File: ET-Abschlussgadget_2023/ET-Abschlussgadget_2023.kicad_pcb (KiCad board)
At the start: 2 copper layers, 85 x 54 mm, 14 parts, among them U1 ATtiny10-TS

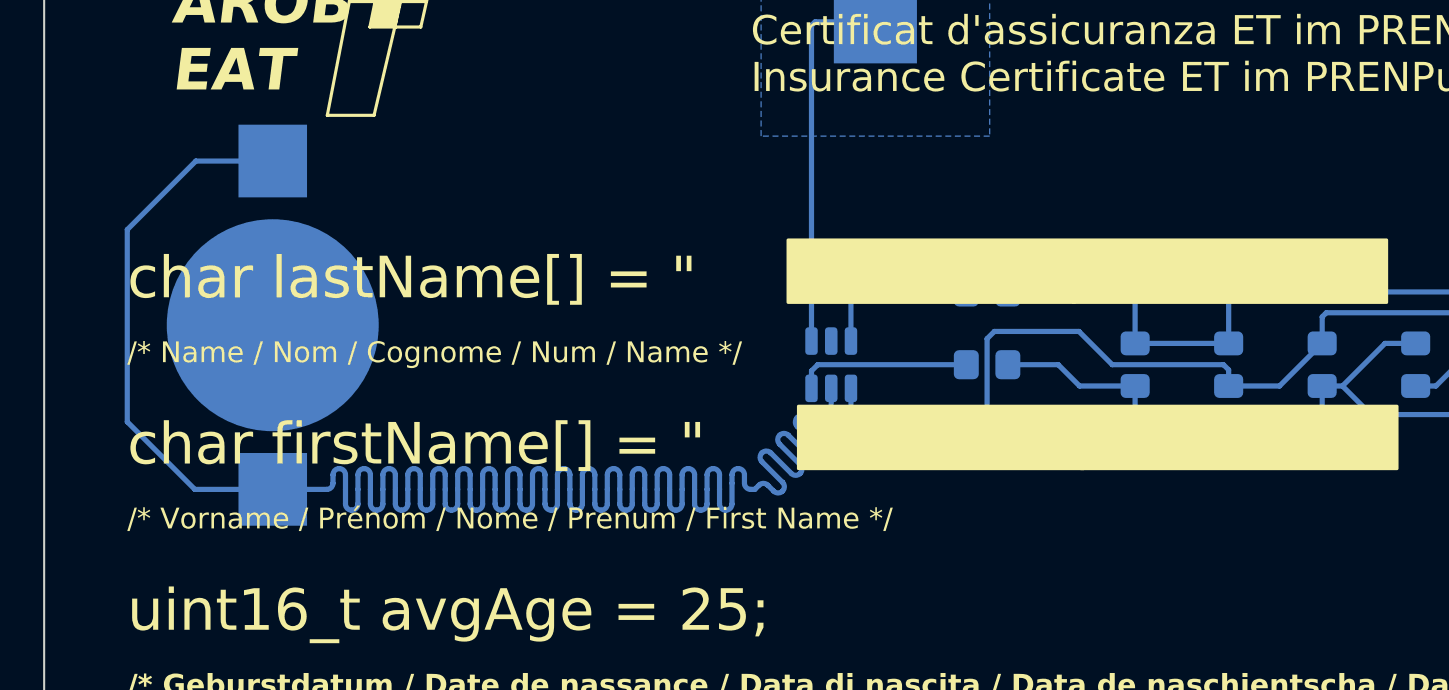
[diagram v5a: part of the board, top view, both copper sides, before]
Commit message: Improve silkscreen
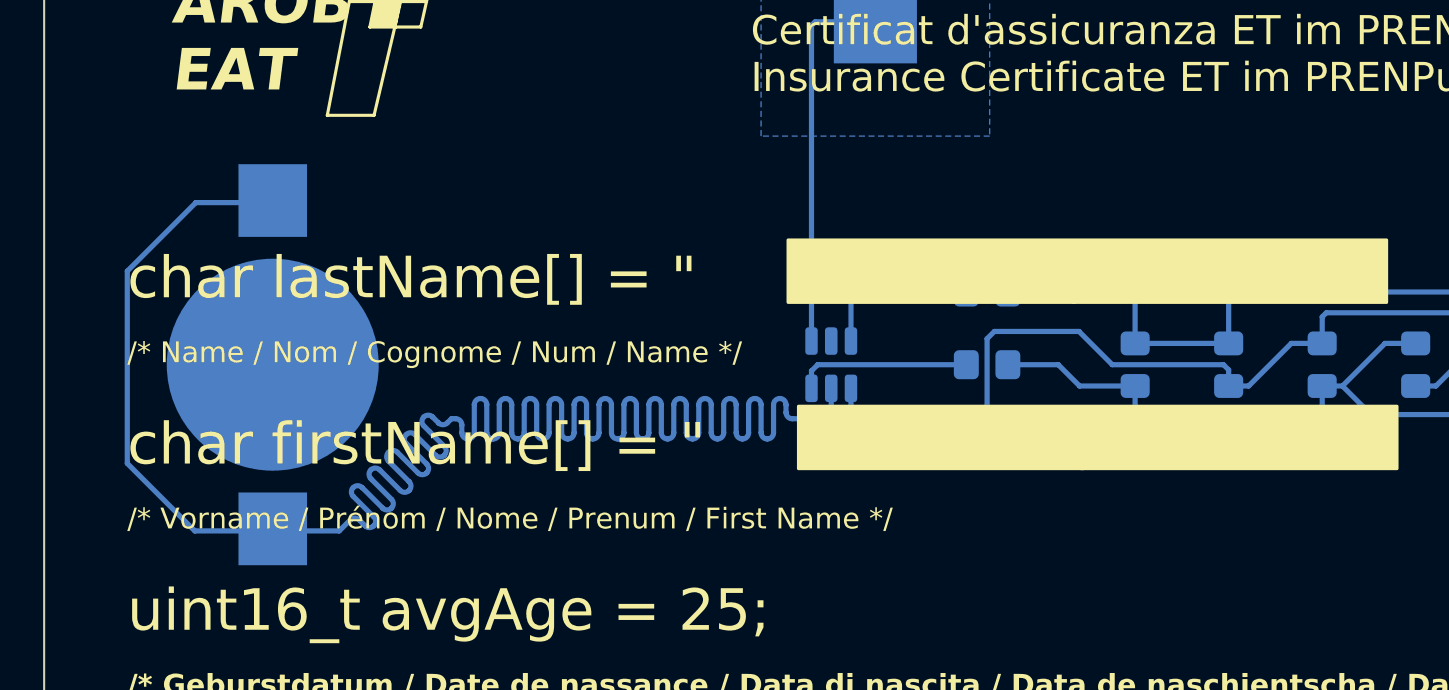
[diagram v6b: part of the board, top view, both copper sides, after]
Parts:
- added kibuzzard-642F1274: G***, kibuzzard-642F1274, B.Cu at (176.6, 107.0)
- added kibuzzard-642F12C7: G***, kibuzzard-642F12C7, B.Cu at (170.5, 102.0)
- added kibuzzard-642F12D5: G***, kibuzzard-642F12D5, B.Cu at (166.0, 102.0)
- added kibuzzard-642F12E3: G***, kibuzzard-642F12E3, B.Cu at (161.5, 102.0)
- added kibuzzard-642F12EF: G***, kibuzzard-642F12EF, B.Cu at (157.0, 102.0)
- added kibuzzard-642F1300: G***, kibuzzard-642F1300, B.Cu at (152.5, 98.0)
- moved G*** 7.28 mm to (128.0, 122.0), turned to 80 degrees
- moved BT1 1.90 mm to (111.0, 107.0)
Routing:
- net VCC: track 122.0 -> 116.3 mm
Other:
- board text removed: "DE"
- board text removed: "ET"
- board text removed: "MEDTECH"
- board text removed: "MT"
- board text removed: "WI"
- board text removed: "WIE ASSI BIST DU?"

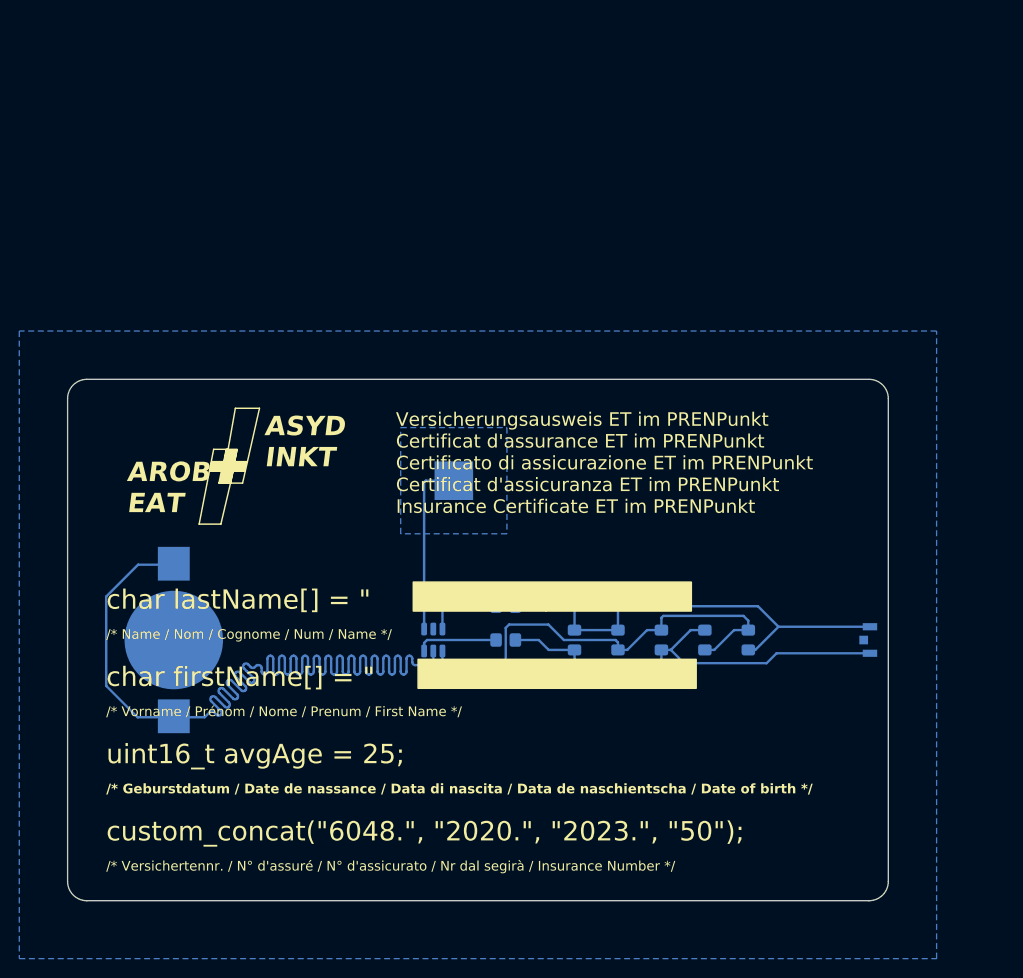
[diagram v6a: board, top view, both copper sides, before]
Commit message: Add inverted banner
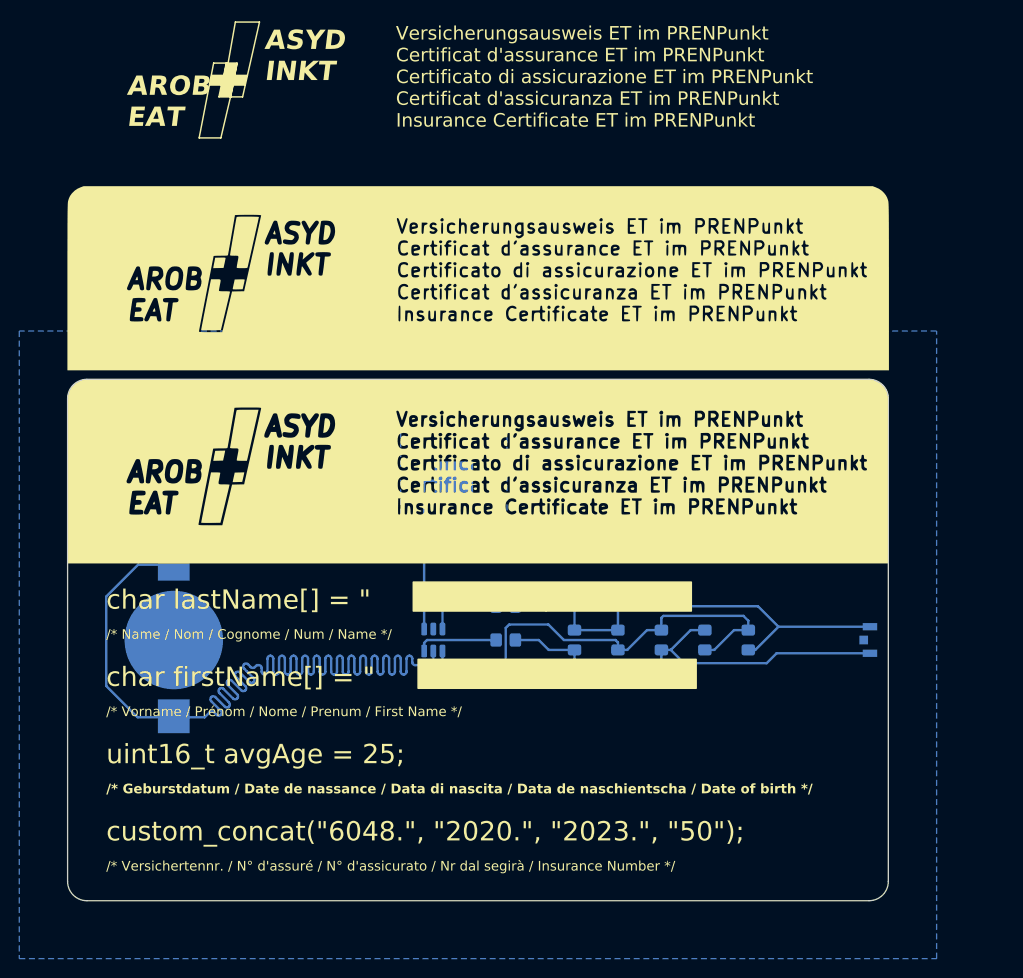
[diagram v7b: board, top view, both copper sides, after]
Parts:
- added G***: LOGO, LOGO, F.Cu at (142.5, 69.5)
- added G***: LOGO, LOGO, F.Cu at (142.5, 89.5)

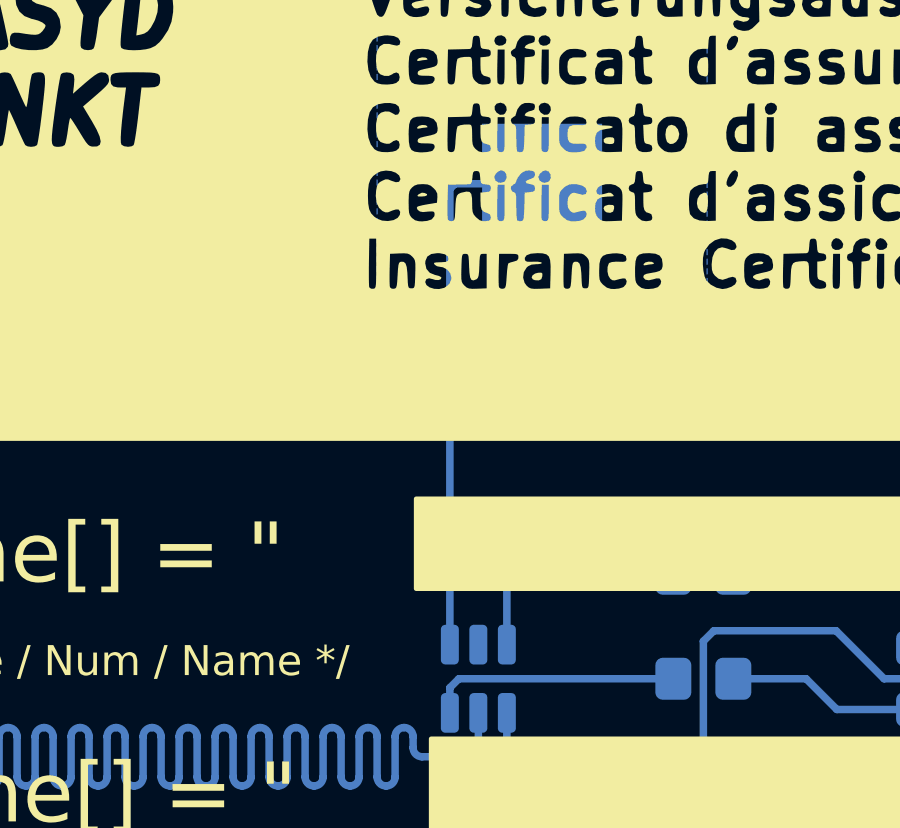
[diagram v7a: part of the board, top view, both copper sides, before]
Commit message: Add series resistor to capacitive pad
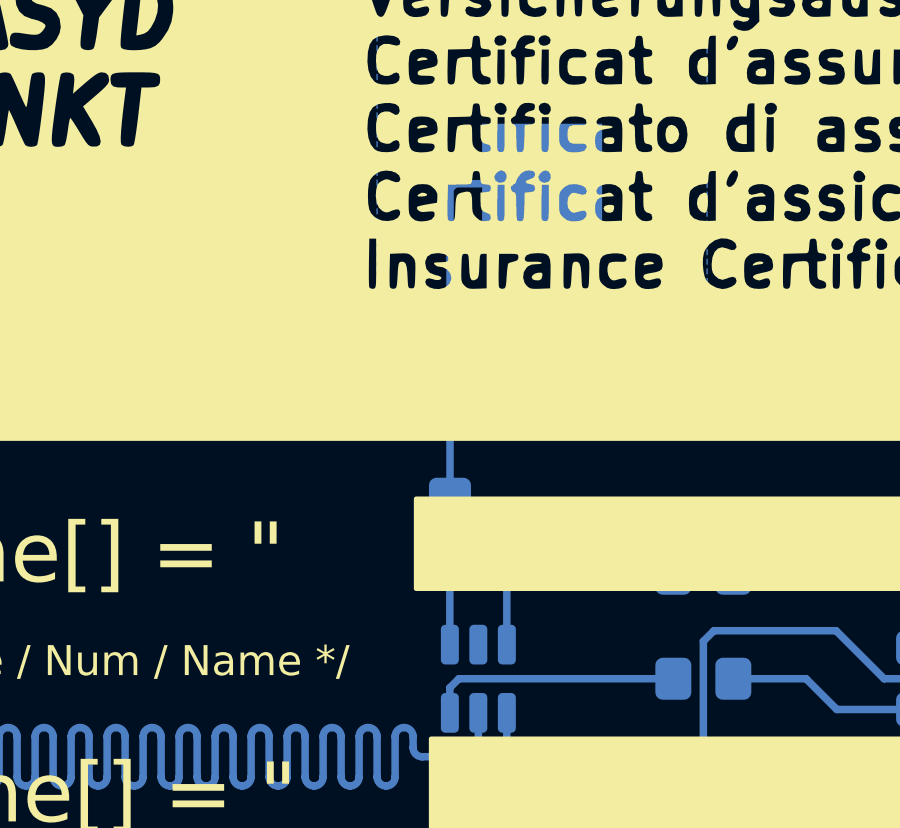
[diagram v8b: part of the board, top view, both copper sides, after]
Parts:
- added R4: 1k, Resistor_SMD:R_0805_2012Metric_Pad1.20x1.40mm_HandSolder, B.Cu at (136.9, 101.9)
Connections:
- U1 pad 1: /Cap_Pad -> Net-(U1-PB0)
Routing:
- net /Cap_Pad: track 18.3 -> 13.4 mm
- net Net-(U1-PB0): track 0.00 -> 2.96 mm
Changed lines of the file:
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@@
   (net 8 "VCC")
   (net 9 "/Cap_Pad")
+  (net 10 "Net-(U1-PB0)")
   (footprint "LOGO" (layer "F.Cu")
     (at 142.5 69.5)
@@
       (stroke (width 0.1) (type solid)) (layer "B.Fab"))
     (pad "1" smd roundrect (at -1.1375 0.95 270) (size 1.325 0.6) (layers "B.Cu" "B.Paste" "B.Mask") (roundrect_rratio 0.25)
-      (net 9 "/Cap_Pad") (pinfunction "PB0") (pintype "bidirectional"))
+      (net 10 "Net-(U1-PB0)") (pinfunction "PB0") (pintype "bidirectional"))
     (pad "2" smd roundrect (at -1.1375 0 270) (size 1.325 0.6) (layers "B.Cu" "B.Paste" "B.Mask") (roundrect_rratio 0.25)
       (net 7 "GND") (pinfunction "GND") (pintype "power_in"))
@@
   )
   (footprint "Resistor_SMD:R_0805_2012Metric_Pad1.20x1.40mm_HandSolder" (layer "B.Cu")
+    (at 136.93 101.9 90)
+    (descr "Resistor SMD 0805 (2012 Metric), square (rectangular) end terminal, IPC_7351 nominal with elongated pad for handsoldering. (Body size source: IPC-SM-782 page 72, https://www.pcb-3d.com/wordpress/wp-content/uploads/ipc-sm-782a_amendment_1_and_2.pdf), generated with kicad-footprint-generator")
+    (tags "resistor handsolder")
+    (property "Sheetfile" "ET-Abschlussgadget_2023.kicad_sch")
+    (property "Sheetname" "")
+    (property "ki_description" "Resistor, small symbol")
+    (property "ki_keywords" "R resistor")
+    (attr smd)
+    (fp_text reference "R4" (at 0 -1.5 270 unlocked) (layer "B.SilkS")
+        (effects (font (size 0.8 0.8) (thickness 0.15)) (justify mirror))
+    )
+    (fp_text value "1k" (at 0 -1.65 90) (layer "B.Fab")
+        (effects (font (size 1 1) (thickness 0.15)) (justify mirror))
+    )
+    (fp_text user "${REFERENCE}" (at 0 0 90) (layer "B.Fab")
+        (effects (font (size 0.5 0.5) (thickness 0.08)) (justify mirror))
+    )
+    (fp_line (start -0.227064 -0.735) (end 0.227064 -0.735)
+      (stroke (width 0.12) (type solid)) (layer "B.SilkS"))
+    (fp_line (start -0.227064 0.735) (end 0.227064 0.735)
+      (stroke (width 0.12) (type solid)) (layer "B.SilkS"))
+    (fp_line (start -1.85 -0.95) (end -1.85 0.95)
+      (stroke (width 0.05) (type solid)) (layer "B.CrtYd"))
+    (fp_line (start -1.85 0.95) (end 1.85 0.95)
+      (stroke (width 0.05) (type solid)) (layer "B.CrtYd"))
+    (fp_line (start 1.85 -0.95) (end -1.85 -0.95)
+      (stroke (width 0.05) (type solid)) (layer "B.CrtYd"))
+    (fp_line (start 1.85 0.95) (end 1.85 -0.95)
+      (stroke (width 0.05) (type solid)) (layer "B.CrtYd"))
+    (fp_line (start -1 -0.625) (end -1 0.625)
+      (stroke (width 0.1) (type solid)) (layer "B.Fab"))
+    (fp_line (start -1 0.625) (end 1 0.625)
+      (stroke (width 0.1) (type solid)) (layer "B.Fab"))
+    (fp_line (start 1 -0.625) (end -1 -0.625)
+      (stroke (width 0.1) (type solid)) (layer "B.Fab"))
+    (fp_line (start 1 0.625) (end 1 -0.625)
+      (stroke (width 0.1) (type solid)) (layer "B.Fab"))
+    (pad "1" smd roundrect (at -1 0 90) (size 1.2 1.4) (layers "B.Cu" "B.Paste" "B.Mask") (roundrect_rratio 0.208333)
+      (net 10 "Net-(U1-PB0)") (pintype "passive"))
+    (pad "2" smd roundrect (at 1 0 90) (size 1.2 1.4) (layers "B.Cu" "B.Paste" "B.Mask") (roundrect_rratio 0.208333)
+      (net 9 "/Cap_Pad") (pintype "passive"))
+    (model "${KICAD6_3DMODEL_DIR}/Resistor_SMD.3dshapes/R_0805_2012Metric.wrl"
+      (offset (xyz 0 0 0))
+      (scale (xyz 1 1 1))
+      (rotate (xyz 0 0 0))
+    )
+  )
+  (footprint "Resistor_SMD:R_0805_2012Metric_Pad1.20x1.40mm_HandSolder" (layer "B.Cu")
     (at 145.375 103.5)
     (descr "Resistor SMD 0805 (2012 Metric), square (rectangular) end terminal, IPC_7351 nominal with elongated pad for handsoldering. (Body size source: IPC-SM-782 page 72, https://www.pcb-3d.com/wordpress/wp-content/uploads/ipc-sm-782a_amendment_1_and_2.pdf), generated with kicad-footprint-generator")
@@
   (arc (start 119.4 109.8) (mid 119.187867 109.887868) (end 118.975734 109.8) (width 0.25) (layer "B.Cu") (net 8))
   (arc (start 126.7 110.272647) (mid 126.612132 110.484779) (end 126.4 110.572647) (width 0.25) (layer "B.Cu") (net 8))
+  (segment (start 136.93 100.9) (end 136.93 90.67) (width 0.25) (layer "B.Cu") (net 9))
+  (segment (start 136.93 90.67) (end 137.1 90.5) (width 0.25) (layer "B.Cu") (net 9))
   (segment (start 137.1 90.5) (end 140 90.5) (width 0.25) (layer "B.Cu") (net 9))
-  (segment (start 136.925 105.8625) (end 136.925 90.675) (width 0.25) (layer "B.Cu") (net 9))
-  (segment (start 136.925 90.675) (end 137.1 90.5) (width 0.25) (layer "B.Cu") (net 9))
+  (segment (start 136.925 105.8625) (end 136.925 102.905) (width 0.25) (layer "B.Cu") (net 10))
+  (segment (start 136.925 102.905) (end 136.93 102.9) (width 0.25) (layer "B.Cu") (net 10))
   (zone (net 7) (net_name "GND") (layer "B.Cu") (hatch edge 0.5)
     (connect_pads yes (clearance 0.5))
